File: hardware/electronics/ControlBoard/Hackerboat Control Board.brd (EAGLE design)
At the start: 114.3 x 195.6 mm, 226 parts, among them IC1 74AHC1G08DBV, IC2 74AUC1G06DBV, IC3 74AHC1G04DBV, U1 IPS6041G, U10 INA169, U11 IPS6041G, U12 INA169, U14 TPS54331, U15 TPS54331, U18 ADC128D818, U19 ADC128D818, U2 IPS6041G, U20 IPS6041G, U21 INA169, U22 IPS6041G, U23 INA169, U24 IPS6041G, U25 INA169, U27 INA169, U29 TPS61175, U3 INA169, U4 IPS6041G, U5 INA169, U6 IPS6041G, U7 INA169, U8 IPS6041G, U9 INA169

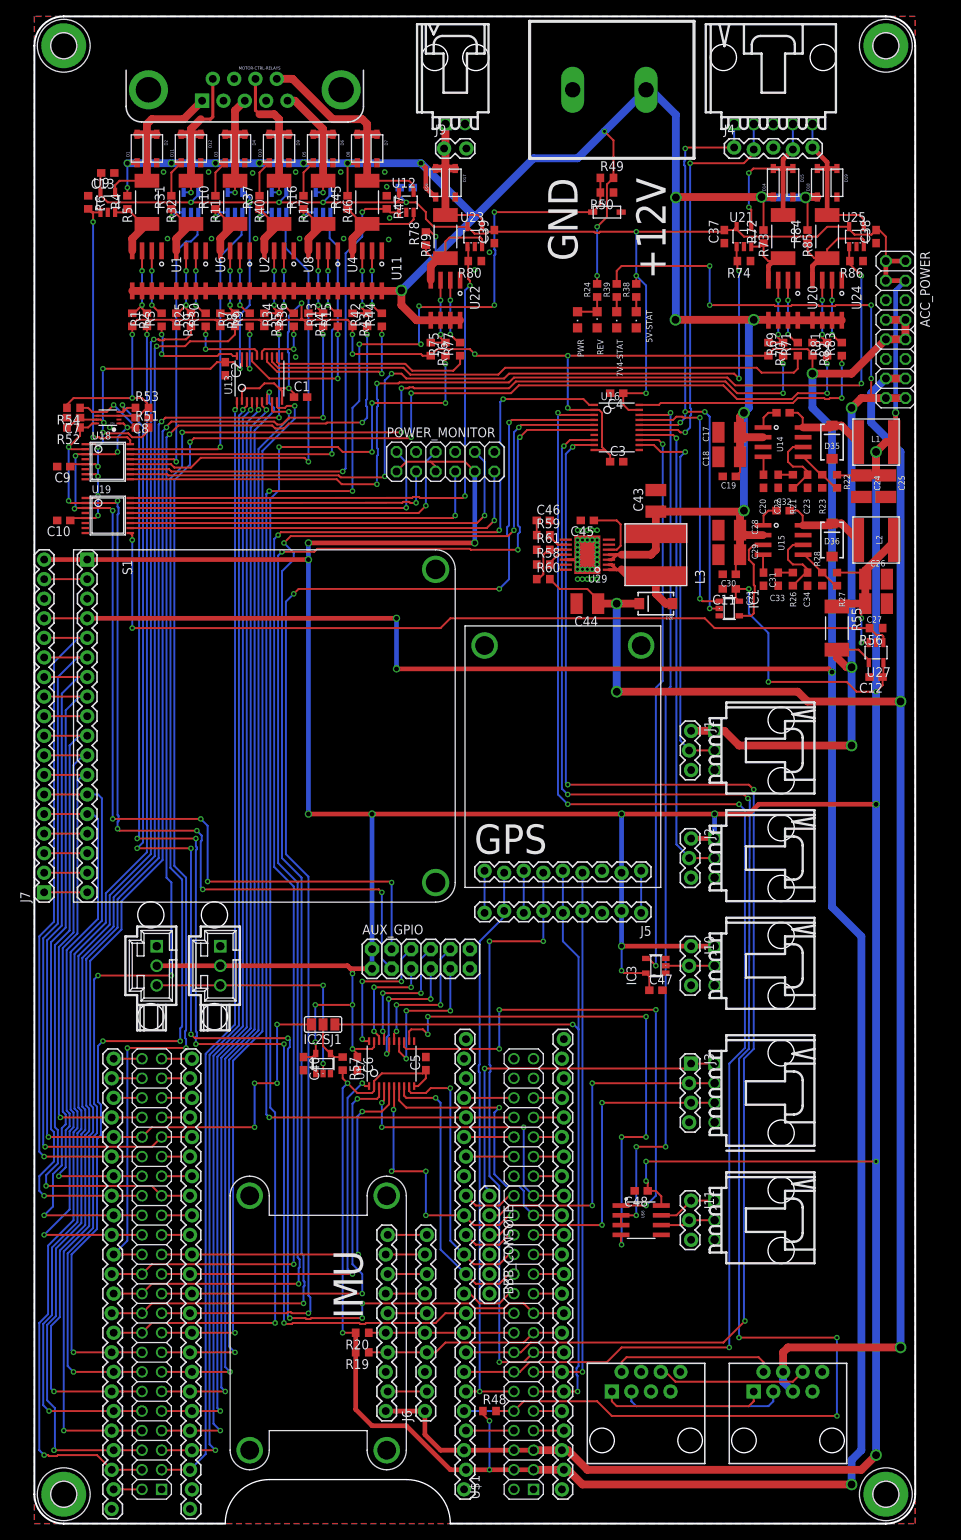
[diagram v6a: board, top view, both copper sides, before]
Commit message: Making sure we have the latest board in github
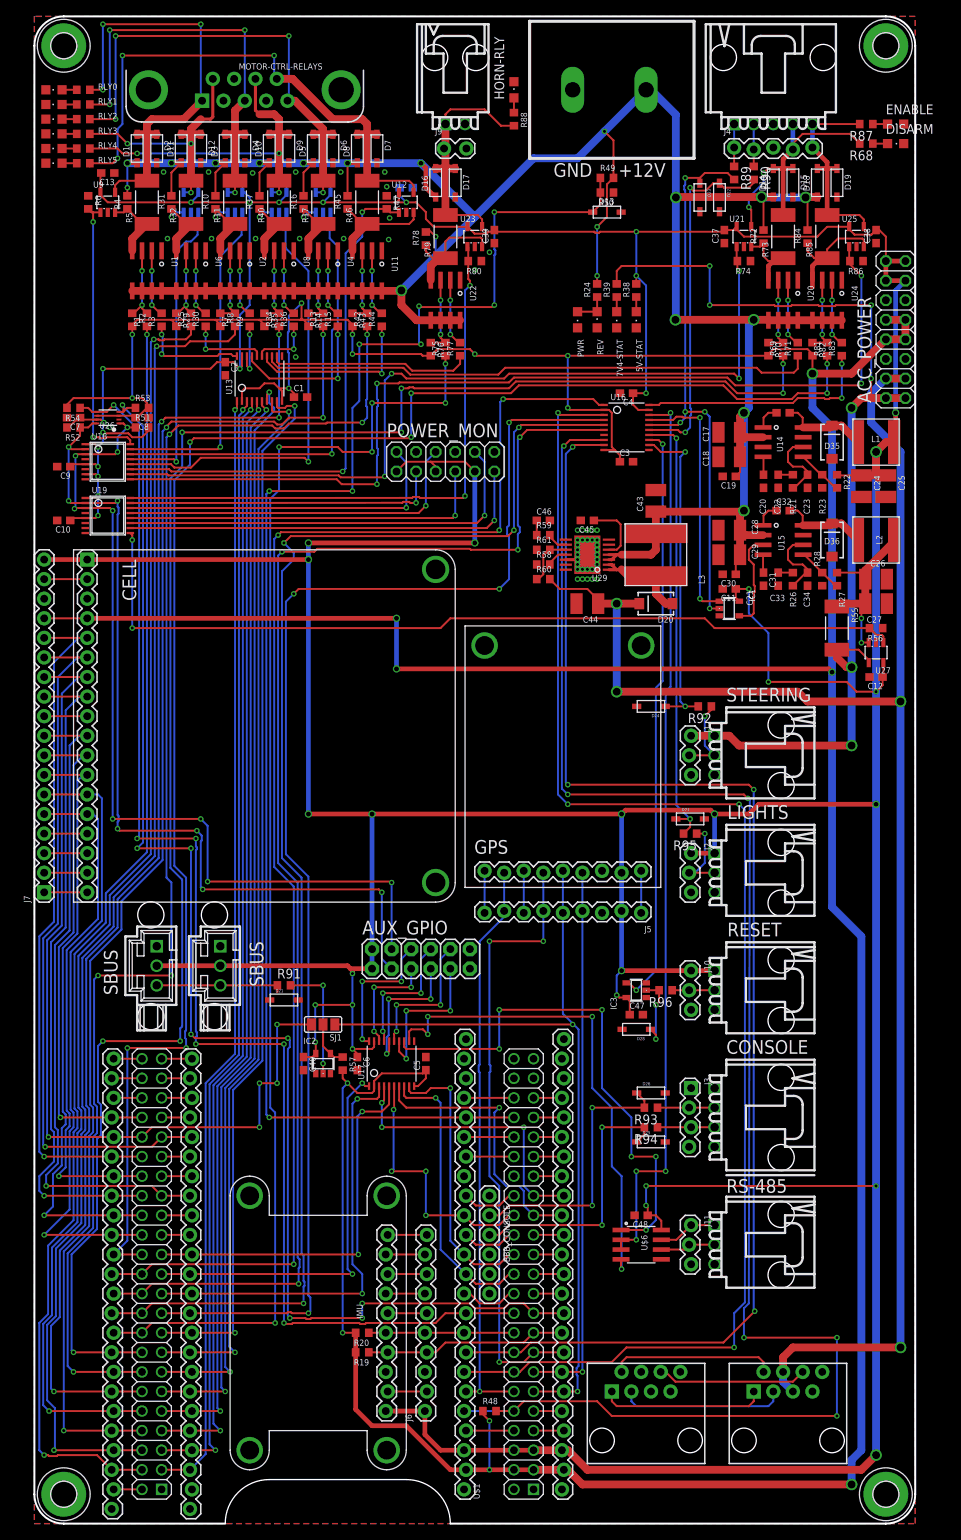
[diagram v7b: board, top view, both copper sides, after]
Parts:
- added D21, D22, D23, D24, D25, D26, D27, D28: 5V, adafruit:SOD-123
- added DISARM: AMB, adafruit:CHIPLED_0805
- added ENABLE, RLY0, RLY1, RLY2, RLY3, RLY4, RLY5: GRN, adafruit:CHIPLED_0805
- added HORN-RLY: RED, adafruit:CHIPLED_0805
- added R62, R63, R64, R65, R66, R67, R68, R87, R88, R89, R90, R91, R92, R93, R94, R95, R96: 1K, resistor:R0603
- 5V-STAT, 7V4-STAT, PWR: value (none) -> GRN
- C40: value (none) -> 100n
- R49: value (none) -> 110K
- R50: value (none) -> 15K
- R57: value (none) -> 10K
- REV: value (none) -> RED
- moved C47 4.07 mm to (78.1, 66.0)
- moved IC3 4.07 mm to (78.1, 69.2)
- moved J10 3.18 mm to (85.1, 71.8)
- moved SERIAL_CONSOLE 3.18 mm to (88.3, 52.7)
- moved BBB_RESET 3.17 mm to (88.3, 69.2)
- moved C48 3.17 mm to (78.7, 40.0)
- moved J11 3.17 mm to (85.1, 38.7)
- moved J3 3.17 mm to (85.1, 56.5)
- moved RS485 3.17 mm to (88.3, 36.2)
- moved U$6 3.17 mm to (78.7, 36.2)
- moved J2 1.91 mm to (85.1, 87.0)
- moved STATUS_LIGHTS 1.91 mm to (88.3, 84.5)
- moved C3 1.27 mm to (76.8, 137.8)
- moved C4 1.27 mm to (76.8, 146.7)
- moved U16 1.27 mm to (76.8, 142.2)
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- renumbered POWER_MONITOR to POWER_MON, S1 to CELL
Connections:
- removed net BBB_UART0_DTR: BBB_CONSOLE.DTR, J3.1, SERIAL_CONSOLE.P$1
- new net N$59: R62.1, RLY0.A
- new net N$60: R63.1, RLY1.A
- new net N$61: R64.1, RLY2.A
- new net N$64: DISARM.A, R68.1
- new net N$65: R65.1, RLY3.A
- new net N$66: R66.1, RLY4.A
- new net N$67: R67.1, RLY5.A
- new net N$71: ENABLE.A, R87.1
- new net N$74: HORN-RLY.A, R88.1
- new net N$87: J4.1, POWER_STATE.P$1, R89.1
- new net N$88: J4.2, POWER_STATE.P$2, R90.1
- new net N$89: J1.2, R92.1, STEERING.P$2
- new net N$90: J3.2, R93.1, SERIAL_CONSOLE.P$2
- new net N$91: J3.3, R94.1, SERIAL_CONSOLE.P$3
- new net N$92: J2.2, R95.1, STATUS_LIGHTS.P$2
- new net N$93: BBB_RESET.P$2, J10.2, R96.1
- new net SBUS_IN_5V: R91.1, SBUS-IN.P$3, SBUS-OUT.P$3
- net BBB_STATUS_LIGHTS_5V: now also D27.C, R95.2; no longer J2.2, STATUS_LIGHTS.P$2
- net BBB_UART0_RX: now also D26.C, R93.2; no longer J3.2, SERIAL_CONSOLE.P$2
- net BBB_UART0_TX: now also D25.C, R94.2; no longer J3.3, SERIAL_CONSOLE.P$3
- net DISARM_RELAY_IN_5V: now also D22.C, R90.2; no longer J4.2, POWER_STATE.P$2
- net ENABLE_RELAY_IN_5V: now also D23.C, R89.2; no longer J4.1, POWER_STATE.P$1
- net GND: now also D21.A, D22.A, D23.A, D24.A, D25.A, D26.A, D27.A, D28.A, DISARM.C, ENABLE.C, HORN-RLY.C, RLY0.C, RLY1.C, RLY2.C, RLY3.C, RLY4.C, RLY5.C
- net N$23: now also D28.C, R96.2; no longer BBB_RESET.P$2, J10.2
- net N$53: now also D21.C, R91.2; no longer SBUS-IN.P$3, SBUS-OUT.P$3
- net RELAY_OUT_0: now also R62.2
- net RELAY_OUT_1: now also R63.2
- net RELAY_OUT_2: now also R64.2
- net RELAY_OUT_3: now also R65.2
- net RELAY_OUT_4: now also R66.2
- net RELAY_OUT_5: now also R67.2
- net RELAY_OUT_DISARM: now also R68.2
- net RELAY_OUT_ENABLE: now also R87.2
- net RELAY_OUT_HORN: now also R88.2
- net SERVO_RUDDER_5V: now also D24.C, R92.2; no longer J1.2, STEERING.P$2
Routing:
- net BBB_UART0_DTR: track 46.9 -> 0.00 mm, vias 1 -> 0
- net RELAY_OUT_2: track 17.9 -> 63.0 mm, vias 1 -> 4
- net RELAY_OUT_5: track 31.3 -> 72.2 mm, vias 0 -> 3
- net RELAY_OUT_1: track 16.0 -> 54.9 mm, vias 1 -> 4
- net RELAY_OUT_0: track 23.6 -> 56.5 mm, vias 0 -> 3
- net RELAY_OUT_4: track 20.7 -> 45.5 mm, vias 1 -> 3
- net N$53: track 33.0 -> 15.7 mm
- net SBUS_IN_5V: track 0.00 -> 16.6 mm
- net RELAY_OUT_3: track 20.2 -> 33.9 mm, vias 1 -> 3
- net RELAY_OUT_HORN: track 20.5 -> 31.8 mm
- net N$92: track 0.00 -> 10.7 mm, vias 0 -> 1
- net N$89: track 0.00 -> 10.5 mm, vias 0 -> 1
- net BBB_UART0_TX: track 45.6 -> 35.7 mm
- net BBB_UART0_RX: track 45.6 -> 35.7 mm
- net RELAY_OUT_DISARM: track 25.4 -> 34.8 mm
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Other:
- board text added: "CONSOLE"
- board text added: "LIGHTS"
- board text added: "RESET"
- board text added: "RS-485"
- board text added: "SBUS"
- board text added: "STEERING"

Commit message: Added mode and dataflow diagrams. Updated board schematic and layout with comments from hardware review.
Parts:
- removed C21: 100n, resistor:C0603
- removed C22: 2n4, resistor:C0603
- removed C23: 56p, resistor:C0603
- removed C24, C25: 22u, resistor:C1210
- removed D35: (no value), ARD-SRG-MOT8-1a:SPARKFUN_SMA-DIODE
- removed L1: 10u, logos-inductors:NR60XX
- removed R21: 26K7, resistor:R0603
- removed R22: 10K2, resistor:R0603
- removed R23: 1K96, resistor:R0603
- removed U14: TPS54331, logos-power:SO08
- added 15V-ENB, SJ2: (no value), jumper:SJ
- added BLOWN, FAULT_0, FAULT_1, FAULT_2, FAULT_3, FAULT_4, FAULT_5, FAULT_DISARM, FAULT_ENABLE, FAULT_HORN: RED, adafruit:CHIPLED_0805
- added C41, C42, C49, C50: 1000p, res-cap-arrays:0805X4-CAP
- added F1, F2: PTC-2920, fuses:2920L
- added IC4: V7805, linear:TO220V
- added IC5: 7805TV, linear:TO220V
- added R100, R101, R102, R103, R104, R105, R106, R107, R108, R109: 1K, resistor:R0603
- added R110, R111, R112, R113: (no value), res-cap-arrays:CTS742C083-RES
- added R97, R98, R99: 10K, resistor:R0603
- added T1: AO4407A, SparkFun-DiscreteSemi:SO08
- C18: value 10u -> 22u
- C19: value 10n -> 10u; device resistor:C0603 -> resistor:C1210
- C20: value 8n2 -> 22u; device resistor:C0603 -> resistor:C1210
- R51, R52, R53, R54: value 4u7 -> 4K7
- moved C20 207.6 mm to (1.27, -50.2), turned to 0 degrees
- moved C19 199.9 mm to (1.27, -43.2), turned to 0 degrees
- moved C18 19.2 mm to (109.2, 141.0), turned to 270 degrees
- moved D13 13.1 mm to (61.6, 167.0), turned to 270 degrees
- moved R50 12.2 mm to (63.5, 167.0), turned to 270 degrees
- moved R49 11.7 mm to (65.4, 167.0), turned to 90 degrees
- moved D21 2.84 mm to (31.1, 65.4)
- moved R91 2.84 mm to (31.1, 67.3)
- moved C17 1.42 mm to (88.9, 141.0), turned to 270 degrees
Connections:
- removed net N$63: C21.1, D35.C, L1.1, U14.8
- removed net N$69: C20.1, U14.4
- removed net N$70: C23.1, R21.2, U14.6
- removed net N$73: R22.1, R23.2, U14.5
- new net N$100: FAULT_0.A, R101.1
- new net N$101: FAULT_1.A, R102.1
- new net N$102: FAULT_2.A, R103.1
- new net N$103: FAULT_3.A, R104.1
- new net N$105: FAULT_4.A, R105.1
- new net N$109: FAULT_5.A, R106.1
- new net N$110: FAULT_ENABLE.A, R107.1
- new net N$111: FAULT_DISARM.A, R108.1
- new net N$112: FAULT_HORN.A, R109.1
- new net N$113: C41.7, R110.1, U18.16
- new net N$114: C41.5, R110.3, U18.15
- new net N$115: C49.7, R112.1, U19.16
- new net N$116: C41.3, R110.5, U18.14
- new net N$118: C41.1, R110.7, U18.13
- new net N$122: C42.7, R111.1, U18.12
- new net N$123: C42.5, R111.3, U18.11
- new net N$124: C42.3, R111.5, U18.10
- new net N$125: C42.1, R111.7, U18.9
- new net N$126: C49.5, R112.3, U19.15
- new net N$127: C49.3, R112.5, U19.14
- new net N$128: C49.1, R112.7, U19.13
- new net N$129: C50.7, R113.1, U19.12
- new net N$130: C50.5, R113.3, U19.11
- new net N$131: C50.3, R113.5, U19.10
- new net N$132: C50.1, R113.7, U19.9
- new net N$94: 15V-ENB.2, L3.1, U29.3, U29.4
- new net N$95: J4.5, POWER_STATE.P$5, SJ2.1
- new net N$96: BLOWN.C, F1.P$2, T1.5, T1.6, T1.7, T1.8
- new net N$97: R99.2, T1.4
- new net N$98: F1.P$1, POWER_INPUT.2, R100.1, R24.2
- new net N$99: BLOWN.A, R100.2
- net +12V: now also 15V-ENB.1, IC4.1, IC5.1, T1.1, T1.2, T1.3; no longer C18.1, L3.1, POWER_INPUT.2, R24.2, U14.2, U29.3, U29.4
- net +5V: now also C18.1, IC4.3, R101.2, R102.2, R103.2, R104.2, R105.2, R106.2, R107.2, R108.2, R109.2; no longer C24.1, C25.1, J2.1, L1.2, R22.2, STATUS_LIGHTS.P$1
- net AUX_ADC_0: now also R113.4; no longer U19.11
- net AUX_ADC_1: now also R113.6; no longer U19.10
- net CHARGE_CURRENT: now also R113.2; no longer U19.12
- net CHARGE_VOLTAGE: now also R112.8; no longer U19.13
- net ENABLE_RELAY_IN_5V: now also R98.1
- net GND: now also C41.2, C41.4, C41.6, C41.8, C42.2, C42.4, C42.6, C42.8, C49.2, C49.4, C49.6, C49.8, C50.2, C50.4, C50.6, C50.8, IC4.2, IC5.2, R97.2, R98.2, R99.1; no longer C22.2, C23.2, C24.2, C25.2, D35.A, R23.1, U14.7
- net MOT_CURRENT: now also R112.4; no longer U19.15
- net MOT_VOLTAGE: now also R112.6; no longer U19.14
- net N$62: now also F2.P$1, J2.1, STATUS_LIGHTS.P$1; no longer C21.2, U14.1
- net N$68: now also C20.1, F2.P$2, IC5.3; no longer C22.1, R21.1
- net RELAY_CURRENT_0: now also R110.2; no longer U18.16
- net RELAY_CURRENT_1: now also R110.4; no longer U18.15
- net RELAY_CURRENT_2: now also R110.6; no longer U18.14
- net RELAY_CURRENT_3: now also R110.8; no longer U18.13
- net RELAY_CURRENT_4: now also R111.2; no longer U18.12
- net RELAY_CURRENT_5: now also R111.4; no longer U18.11
- net RELAY_CURRENT_DISARM: now also R111.6; no longer U18.10
- net RELAY_CURRENT_ENABLE: now also R111.8; no longer U18.9
- net RELAY_CURRENT_HORN: now also R112.2; no longer U19.16
- net RELAY_DISARM_FAULT: now also FAULT_DISARM.C
- net RELAY_ENABLE_FAULT: now also FAULT_ENABLE.C
- net RELAY_FAULT_0: now also FAULT_0.C
- net RELAY_FAULT_1: now also FAULT_1.C
- net RELAY_FAULT_2: now also FAULT_2.C
- net RELAY_FAULT_3: now also FAULT_3.C
- net RELAY_FAULT_4: now also FAULT_4.C
- net RELAY_FAULT_5: now also FAULT_5.C
- net RELAY_HORN_FAULT: now also FAULT_HORN.C
- net RELAY_OUT_ENABLE: now also SJ2.2; no longer J4.5, POWER_STATE.P$5
- net SERVO_CURRENT_MON: now also R113.8; no longer U19.9
- net SERVO_ENABLE_5V: now also R97.1
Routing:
- net +12V: track 357.1 -> 310.6 mm, vias 20 -> 18
- net N$98: track 0.00 -> 38.8 mm, vias 0 -> 2
- net RELAY_ENABLE_FAULT: track 214.2 -> 247.8 mm, vias 7 -> 8
- net RELAY_DISARM_FAULT: track 231.4 -> 264.5 mm, vias 8 -> 9
- net RELAY_FAULT_2: track 179.3 -> 204.7 mm, vias 4 -> 7
- net N$96: track 0.00 -> 25.2 mm, vias 0 -> 2
- net RELAY_FAULT_5: track 181.6 -> 205.9 mm, vias 6 -> 9
- net RELAY_HORN_FAULT: track 170.2 -> 192.9 mm, vias 6 -> 8
- net RELAY_FAULT_4: track 171.0 -> 191.1 mm, vias 4 -> 7
- net RELAY_FAULT_1: track 173.2 -> 189.2 mm, vias 2 -> 4
- net N$94: track 0.00 -> 15.1 mm
- net SERVO_CURRENT_MON: track 112.2 -> 98.3 mm
- net RELAY_FAULT_0: track 166.4 -> 180.1 mm, vias 2 -> 3
- net N$130: track 0.00 -> 12.9 mm, vias 0 -> 1
- net N$118: track 0.00 -> 12.9 mm, vias 0 -> 1
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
